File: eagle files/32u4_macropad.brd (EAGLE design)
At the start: 75.2 x 98.6 mm, 90 parts, among them J1 TYPE-C-31-M-12, Q1 16Mhz, SW2 SWITCH-SMD-EVP-BB2A9B00

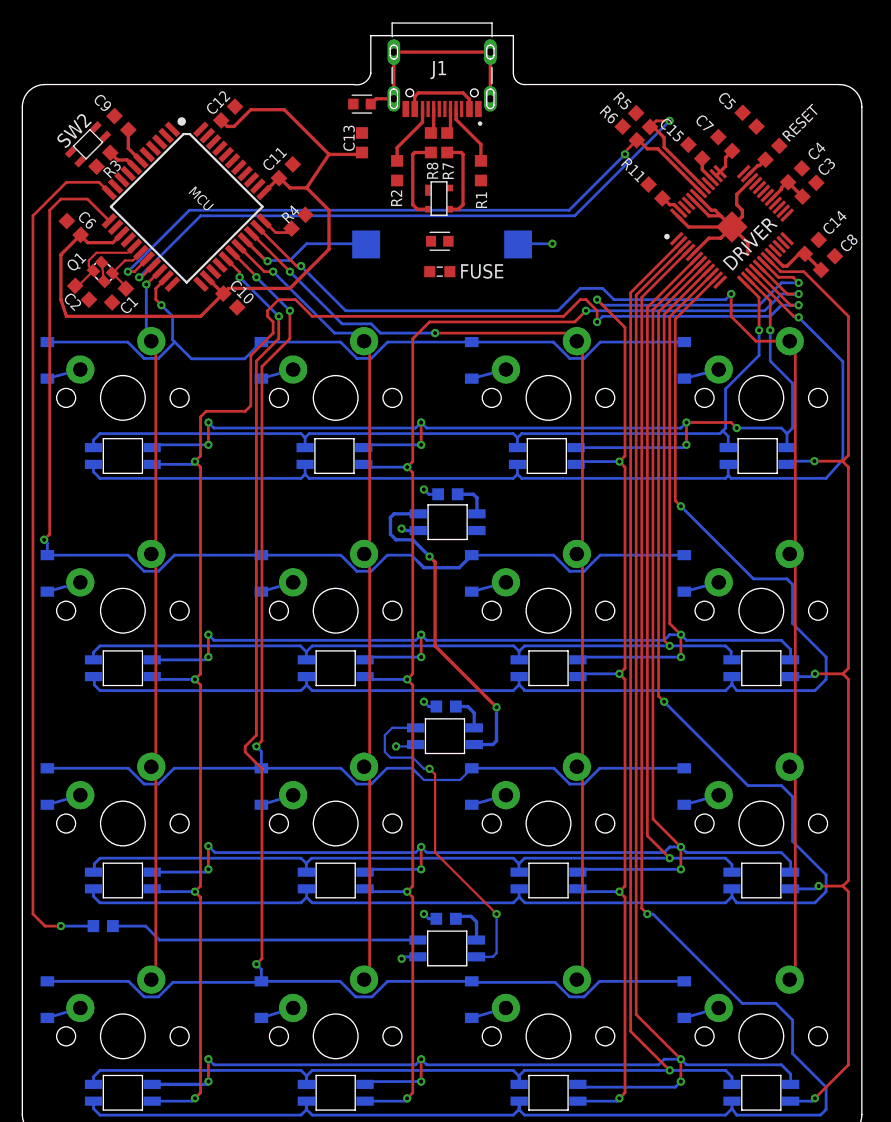
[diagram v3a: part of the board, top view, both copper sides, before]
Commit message: Board USB are work, minor fixes
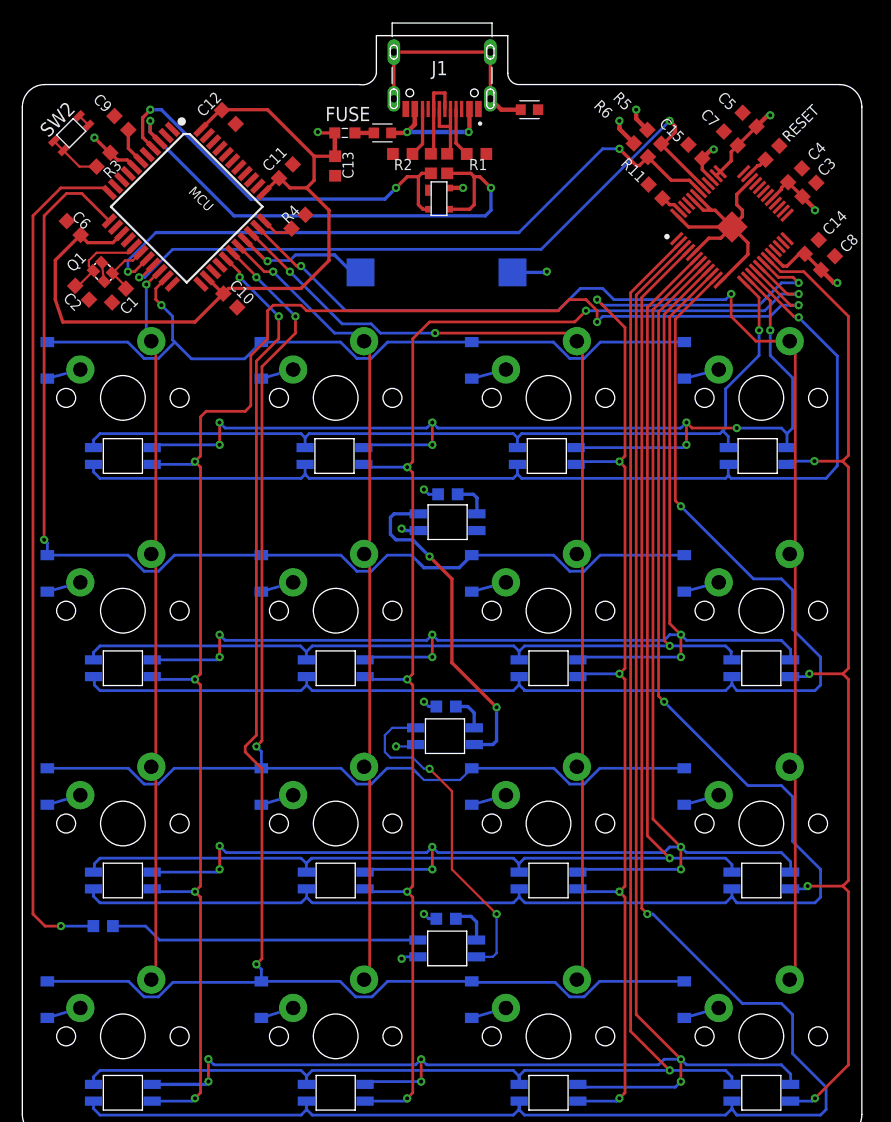
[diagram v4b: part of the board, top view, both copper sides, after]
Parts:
- removed FB1, FB2: FERRITE_BEAD, Filter:BEADC1608X95N
- added FERRITE_USB, FERRITE_VCC: FERRITE_BEAD, Filter:BEADC1608X95N
- moved FUSE 15.1 mm to (38.9, 99.9)
- moved C13 3.18 mm to (38.0, 97.0), turned to 270 degrees
- moved SP1 2.55 mm to (47.1, 87.4)
- moved R7 1.86 mm to (48.1, 97.2)
- moved R8 1.86 mm to (46.6, 97.2)
- moved R5 1.80 mm to (66.6, 99.6)
- moved R6 1.80 mm to (65.4, 98.4)
- moved SW2 1.80 mm to (14.4, 99.9)
- moved R2 1.58 mm to (44.1, 98.0), turned to 0 degrees
- moved R1 1.55 mm to (50.7, 98.0), turned to 180 degrees
- moved C7 0.71 mm to (73.5, 99.4)
- moved C12 0.32 mm to (28.5, 101.3), turned to 315 degrees
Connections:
- removed net N$15: J1.B5, R2.2
- removed net N$2: J1.A5, R1.2
- removed net N$22: FB2.1, J1.S1, J1.S2, J1.S3, J1.S4
- new net VBUS: FERRITE_VCC.2, FUSE.2
- net GND: now also FERRITE_USB.2; no longer C1.1, C10.2, C11.2, C12.2, C13.2, C14.1, C15.1, C19.1, C2.1, C20.1, C21.1, C3.1, C4.1, C5.1, C6.2, C7.1, C8.1, C9.1, DRIVER.12, DRIVER.34, DRIVER.43, DRIVER.44, DRIVER.48, DRIVER.49, DRIVER.5, FB2.2, Q1.2, Q1.4, R11.1, RESET.2, SW2.A@1, SW2.A@2, U$1.1, UGLOW1.P$3, UGLOW2.P$3, UGLOW3.P$3
- net N$24: now also C1.1, C10.2, C11.2, C12.2, C13.2, C14.1, C15.1, C19.1, C2.1, C20.1, C21.1, C3.1, C4.1, C5.1, C6.2, C7.1, C8.1, C9.1, DRIVER.12, DRIVER.34, DRIVER.43, DRIVER.44, DRIVER.48, DRIVER.49, DRIVER.5, FERRITE_USB.1, J1.A5, J1.B5, J1.S1, J1.S2, J1.S3, J1.S4, Q1.2, Q1.4, R1.2, R11.1, R2.2, RESET.2, SW2.A@1, SW2.A@2, U$1.1, UGLOW1.P$3, UGLOW2.P$3, UGLOW3.P$3; no longer FB1.2, FUSE.2
- net VUSB: now also FERRITE_VCC.1; no longer FB1.1
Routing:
- net N$24: track 0.00 -> 69.4 mm, vias 0 -> 6
- net D-: track 7.36 -> 48.4 mm, vias 0 -> 2
- net GND: track 36.5 -> 0.00 mm, vias 6 -> 0
- net D+: track 7.76 -> 37.1 mm, vias 0 -> 2
- net N$22: track 19.3 -> 0.00 mm
- net VCC: track 92.3 -> 111.3 mm, vias 0 -> 7
- net N$18: track 2.25 -> 7.98 mm
- net N$15: track 5.59 -> 0.00 mm
- net N$2: track 5.57 -> 0.00 mm
- net VUSB: track 7.25 -> 12.7 mm, vias 0 -> 3
- net N$17: track 0.00 -> 4.76 mm
- net N$14: track 2.27 -> 6.69 mm
- net VCC1: track 5.94 -> 7.87 mm, vias 0 -> 1
- net VBUS: track 0.00 -> 1.69 mm
- net C0RGB: track 149.0 -> 147.8 mm
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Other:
- outline, holes or cut-outs redrawn

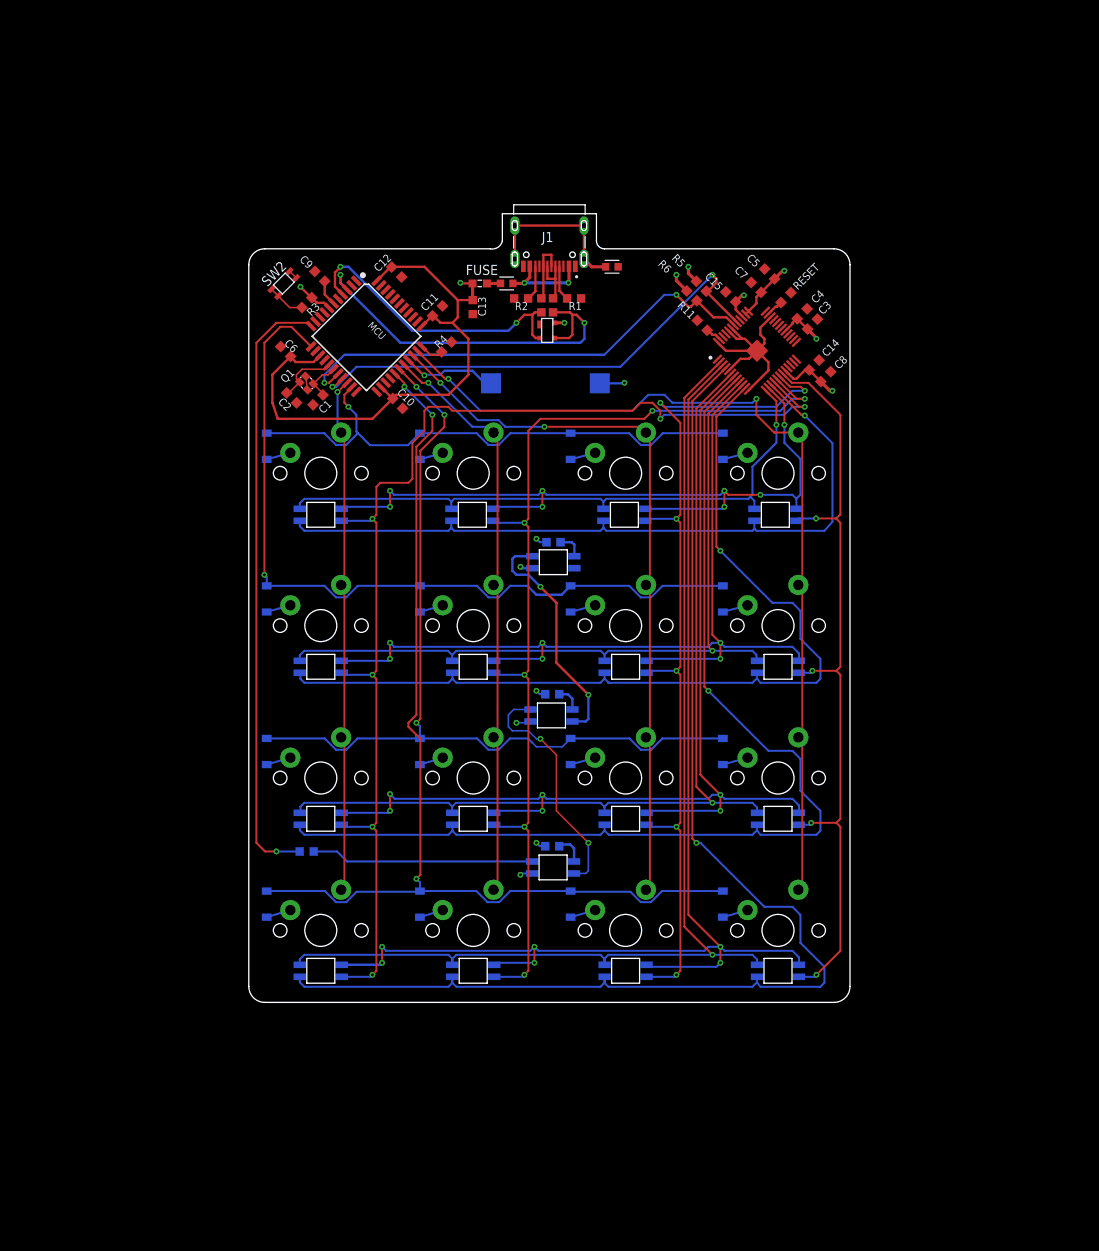
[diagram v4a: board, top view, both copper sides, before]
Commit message: GND net fixes, drc checks, other fixes
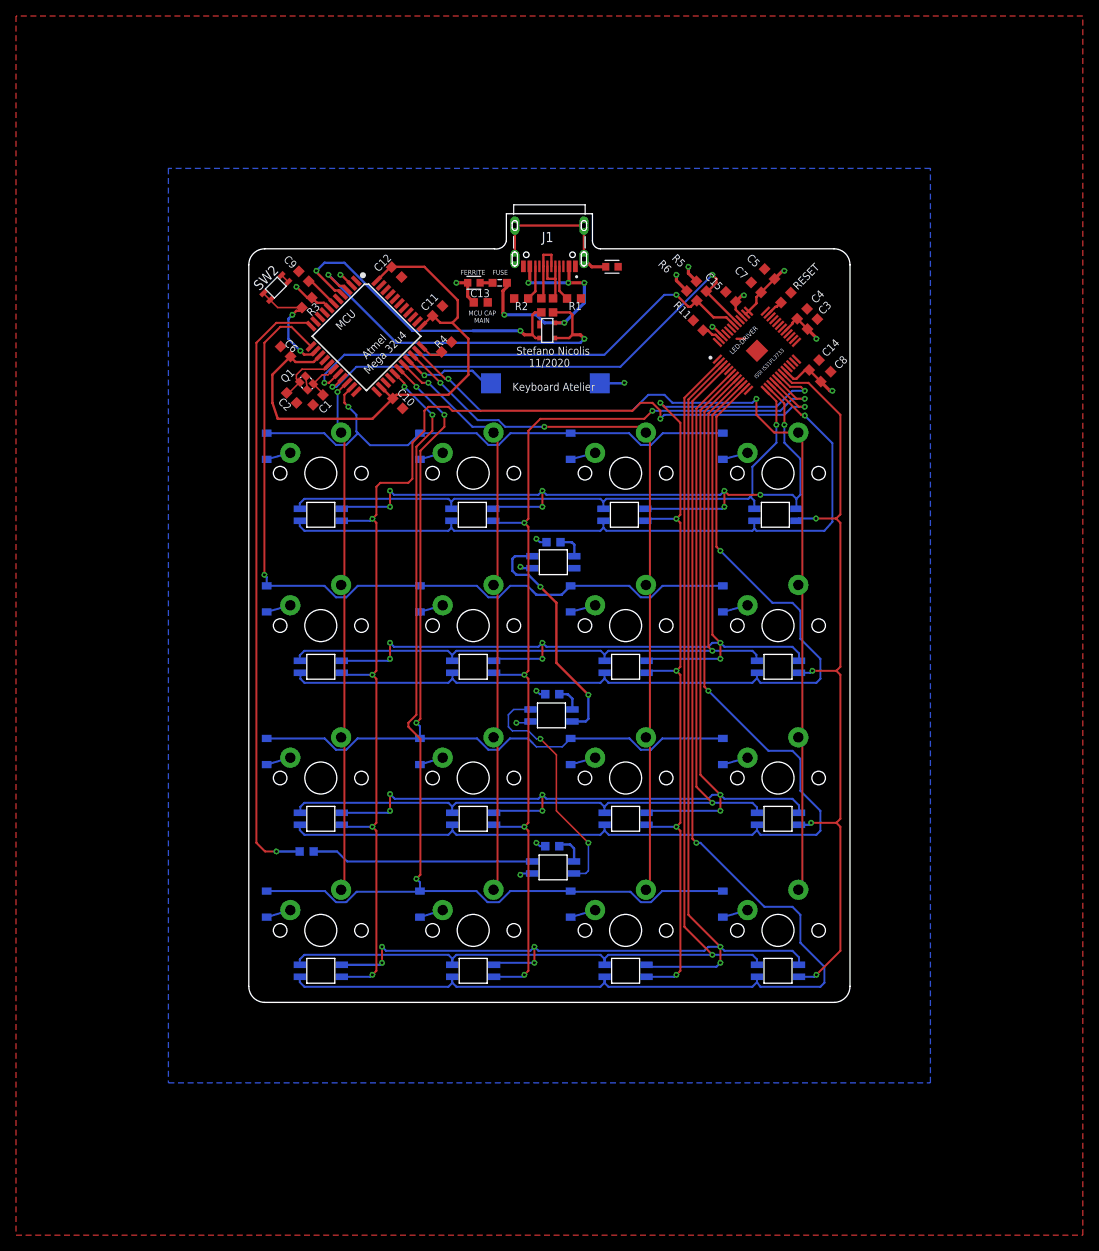
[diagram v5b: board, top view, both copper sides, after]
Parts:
- moved FERRITE_VCC 4.10 mm to (38.2, 100.0)
- moved FUSE 2.50 mm to (41.4, 100.0)
- moved C9 2.00 mm to (16.9, 100.8)
- moved C13 1.15 mm to (39.0, 97.5), turned to 0 degrees
- moved SW2 1.12 mm to (13.4, 99.4)
- moved R11 0.50 mm to (66.2, 94.7)
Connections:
- removed net N$40: SP1.-
- removed net VUSB: FERRITE_VCC.1, J1.A4B9, J1.B4A9, U$1.4
- new net N$2: FERRITE_VCC.1, FUSE.1
- net GND: now also C1.1, C10.2, C11.2, C12.2, C13.2, C14.1, C15.1, C19.1, C2.1, C20.1, C21.1, C3.1, C4.1, C5.1, C6.2, C7.1, C8.1, C9.1, DRIVER.12, DRIVER.34, DRIVER.43, DRIVER.44, DRIVER.48, DRIVER.49, DRIVER.5, Q1.2, Q1.4, R11.1, RESET.2, SP1.-, SW2.A@1, SW2.A@2, U$1.1, UGLOW1.P$3, UGLOW2.P$3, UGLOW3.P$3
- net N$24: no longer C1.1, C10.2, C11.2, C12.2, C13.2, C14.1, C15.1, C19.1, C2.1, C20.1, C21.1, C3.1, C4.1, C5.1, C6.2, C7.1, C8.1, C9.1, DRIVER.12, DRIVER.34, DRIVER.43, DRIVER.44, DRIVER.48, DRIVER.49, DRIVER.5, Q1.2, Q1.4, R11.1, RESET.2, SW2.A@1, SW2.A@2, U$1.1, UGLOW1.P$3, UGLOW2.P$3, UGLOW3.P$3
- net VBUS: now also J1.A4B9, J1.B4A9, U$1.4; no longer FERRITE_VCC.2
- net VCC: now also FERRITE_VCC.2; no longer FUSE.1
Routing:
- net N$24: track 69.4 -> 29.2 mm, vias 6 -> 0
- net VBUS: track 1.69 -> 30.8 mm, vias 0 -> 5
- net GND: track 0.00 -> 16.0 mm, vias 0 -> 7
- net VUSB: track 12.7 -> 0.00 mm, vias 3 -> 0
- net N$17: track 4.76 -> 14.8 mm, vias 0 -> 2
- net D+: track 37.1 -> 40.6 mm
- net N$40: track 3.10 -> 0.00 mm, vias 1 -> 0
- net VCC: track 111.3 -> 114.1 mm, vias 7 -> 9
- net N$2: track 0.00 -> 1.56 mm
- net N$20: track 3.24 -> 4.28 mm
- net N$10: track 2.11 -> 2.61 mm
- added copper zone on layer 1, net GND
- added copper zone on layer 16, net VCC
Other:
- outline, holes or cut-outs redrawn
- board text added: "Atmel Mega 32u4"
- board text added: "FERRITE"
- board text added: "FUSE"
- board text added: "ISSI IS31FL3733"
- board text added: "Keyboard Atelier"
- board text added: "LED-DRIVER"
- board text added: "MCU"
- board text added: "MCU CAP MAIN"
- board text added: "Stefano Nicolis 11/2020"

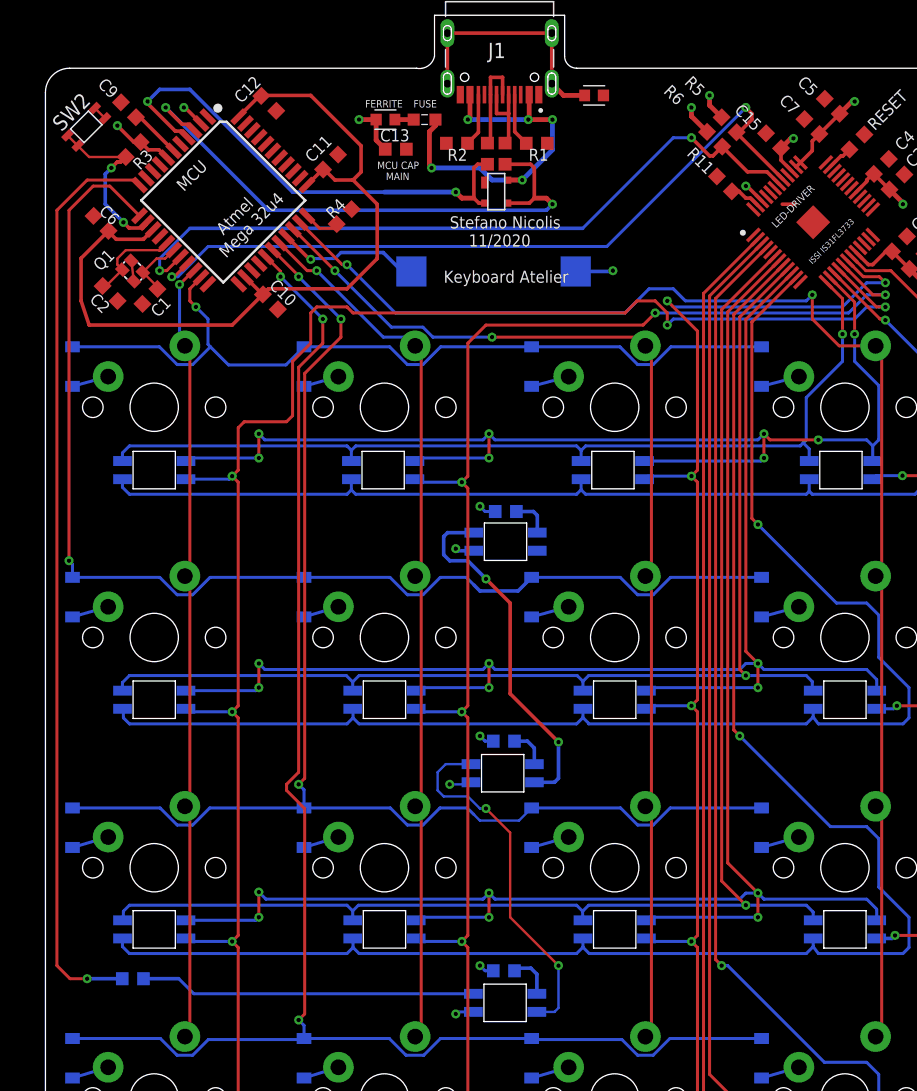
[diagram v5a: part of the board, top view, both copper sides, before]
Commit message: ESD routing fix and finished, usb data line resistors moved after ESD, minor fixes
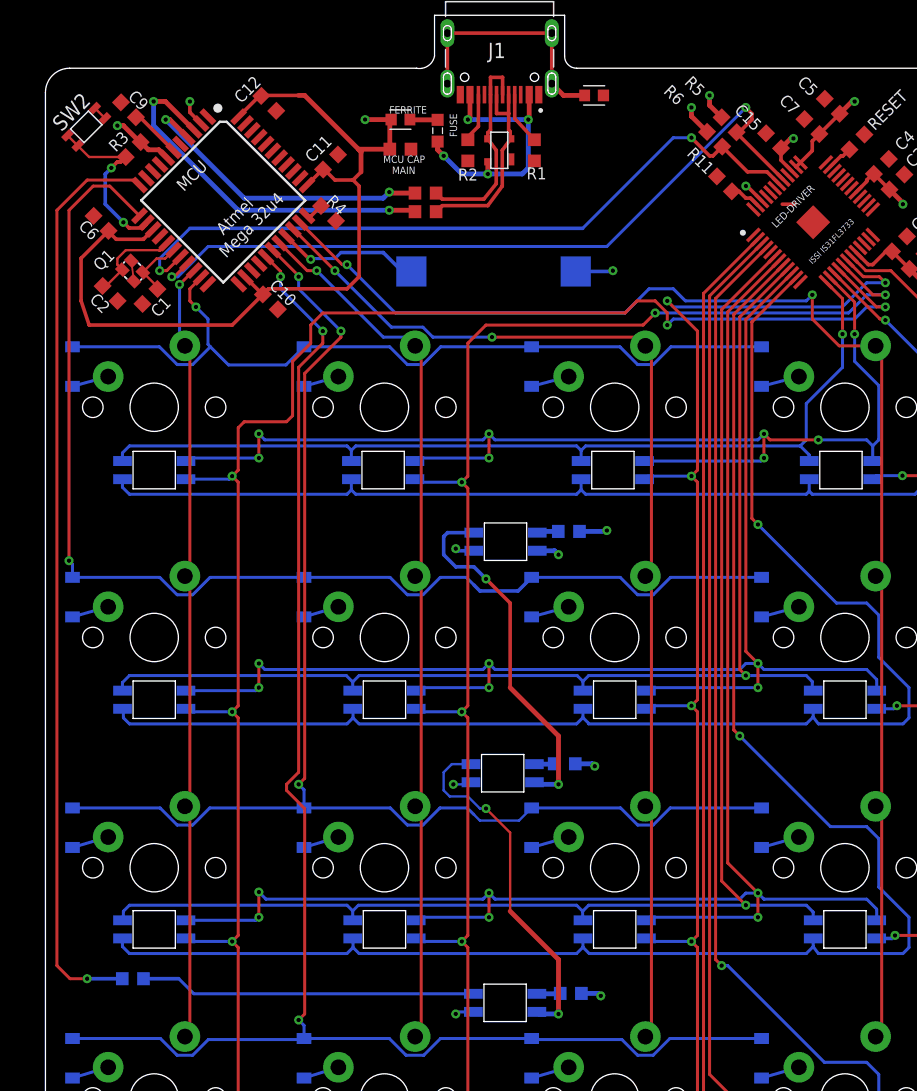
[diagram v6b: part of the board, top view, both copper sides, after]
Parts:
- moved R7 7.34 mm to (41.5, 93.9), turned to 180 degrees
- moved R8 7.02 mm to (41.5, 92.4), turned to 180 degrees
- moved C21 5.84 mm to (53.5, 27.7), turned to 0 degrees
- moved C19 5.47 mm to (53.4, 65.9), turned to 0 degrees
- moved C20 5.37 mm to (53.0, 46.7), turned to 0 degrees
- moved U$1 3.43 mm to (47.6, 97.5), turned to 90 degrees
- moved FUSE 1.42 mm to (42.5, 99.1), turned to 270 degrees
- moved R4 1.32 mm to (33.5, 92.2), turned to 135 degrees
- moved FERRITE_VCC 1.24 mm to (39.4, 100.0)
- moved R2 1.07 mm to (45.0, 97.5), turned to 90 degrees
- moved R1 0.62 mm to (50.5, 97.5), turned to 90 degrees
- moved C13 0.38 mm to (39.4, 97.5)
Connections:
- removed net N$14: J1.A7, J1.B7, R7.1
- removed net N$18: J1.A6, J1.B6, R8.1
- new net N$15: MCU.4, R7.2
- new net N$6: MCU.3, R8.2
- net D+: now also J1.A6, J1.B6, R7.1, U$1.3; no longer MCU.4, R8.2, U$1.2
- net D-: now also J1.A7, J1.B7, R8.1, U$1.2; no longer MCU.3, R7.2, U$1.3
- net GND: now also UGLOW3.P$2
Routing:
- net D-: track 48.0 -> 16.9 mm, vias 2 -> 0
- net N$6: track 0.00 -> 30.9 mm, vias 0 -> 2
- net N$15: track 0.00 -> 26.0 mm, vias 0 -> 2
- net D+: track 40.6 -> 17.4 mm, vias 2 -> 0
- net N$18: track 7.98 -> 0.00 mm
- net VBUS: track 30.8 -> 23.5 mm, vias 5 -> 4
- net N$14: track 6.69 -> 0.00 mm
- net GND: track 16.0 -> 19.3 mm, vias 7 -> 8
- net VCC: track 114.1 -> 111.0 mm
- net N$8: track 3.15 -> 1.50 mm
- net C0RGB: track 147.8 -> 146.8 mm
- net N$2: track 1.56 -> 2.30 mm
- net N$39: track 30.1 -> 29.5 mm
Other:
- board text removed: "Keyboard Atelier"
- board text removed: "Stefano Nicolis 11/2020"

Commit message: Routing fixes
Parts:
- removed UGLOW3: SK6812MINI-E, SK6812MINI-E:SK6812MINI-E
- added C16: 100nF, Components:C0603
- added SK6812MINI-E: SK6812MINI-E, SK6812MINI-E:SK6812MINI-E
- C19, C20, C21: value 100uF -> 100nF
- Q1: value 16Mhz -> 16MHz
- moved FERRITE_VCC 12.4 mm to (48.5, 91.6), turned to 270 degrees
- moved C19 11.7 mm to (41.6, 65.6), turned to 180 degrees
- moved C13 10.2 mm to (40.0, 87.4), turned to 270 degrees
- moved FUSE 8.46 mm to (46.5, 91.6), turned to 90 degrees
- moved R3 4.18 mm to (13.4, 96.0), turned to 180 degrees
- moved R2 2.15 mm to (43.5, 99.0), turned to 0 degrees
- moved R7 2.00 mm to (41.5, 95.9)
- moved R8 2.00 mm to (41.5, 94.4)
- moved R11 2.00 mm to (65.8, 92.7), turned to 45 degrees
- moved R1 1.83 mm to (51.5, 99.0), turned to 180 degrees
- moved C9 1.80 mm to (18.4, 99.8)
- moved C14 1.12 mm to (79.7, 89.2)
- moved C5 1.12 mm to (74.6, 100.1)
- moved C6 1.12 mm to (15.2, 90.4)
- moved U$1 1.00 mm to (47.6, 98.5)
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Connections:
- removed net VCC1: C14.2, C8.2, DRIVER.20
- net AUDIO: now also C16.1, MCU.31; no longer MCU.30
- net C2SWTCH: now also MCU.30; no longer MCU.31
- net GND: now also C16.2, SK6812MINI-E.P$3; no longer UGLOW3.P$2, UGLOW3.P$3
- net N$25: now also SK6812MINI-E.P$4; no longer UGLOW3.P$4
- net VCC: now also C14.2, C8.2, DRIVER.20, SK6812MINI-E.P$1; no longer UGLOW3.P$1
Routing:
- net VCC: track 111.0 -> 305.6 mm, vias 9 -> 16
- net C0RGB: track 146.8 -> 220.6 mm
- net GND: track 19.3 -> 49.3 mm, vias 8 -> 12
- net VCC1: track 7.87 -> 0.00 mm, vias 1 -> 0
- net N$25: track 30.0 -> 23.2 mm
- net C3RGB: track 98.8 -> 94.1 mm
- net C2RGB: track 112.4 -> 109.5 mm
- net N$6: track 30.9 -> 28.1 mm
- net C3SWTCH: track 113.5 -> 110.7 mm
- net N$15: track 26.0 -> 23.3 mm
- net VBUS: track 23.5 -> 21.1 mm
- net R1SWTCH: track 99.7 -> 97.3 mm
- net N$20: track 4.28 -> 2.45 mm
- net R3GREEN: track 156.4 -> 158.1 mm
- net N$17: track 14.8 -> 13.2 mm
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- removed copper zone on layer 16, net VCC
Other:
- board text added: "BOOT"
